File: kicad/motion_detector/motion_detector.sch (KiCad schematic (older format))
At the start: 20 parts, among them SW1 SW_Push, U1 MPU9250, U2 AE-FT234X, U3 pic16f18326, U4 tactile_sw, U5 EEPROM

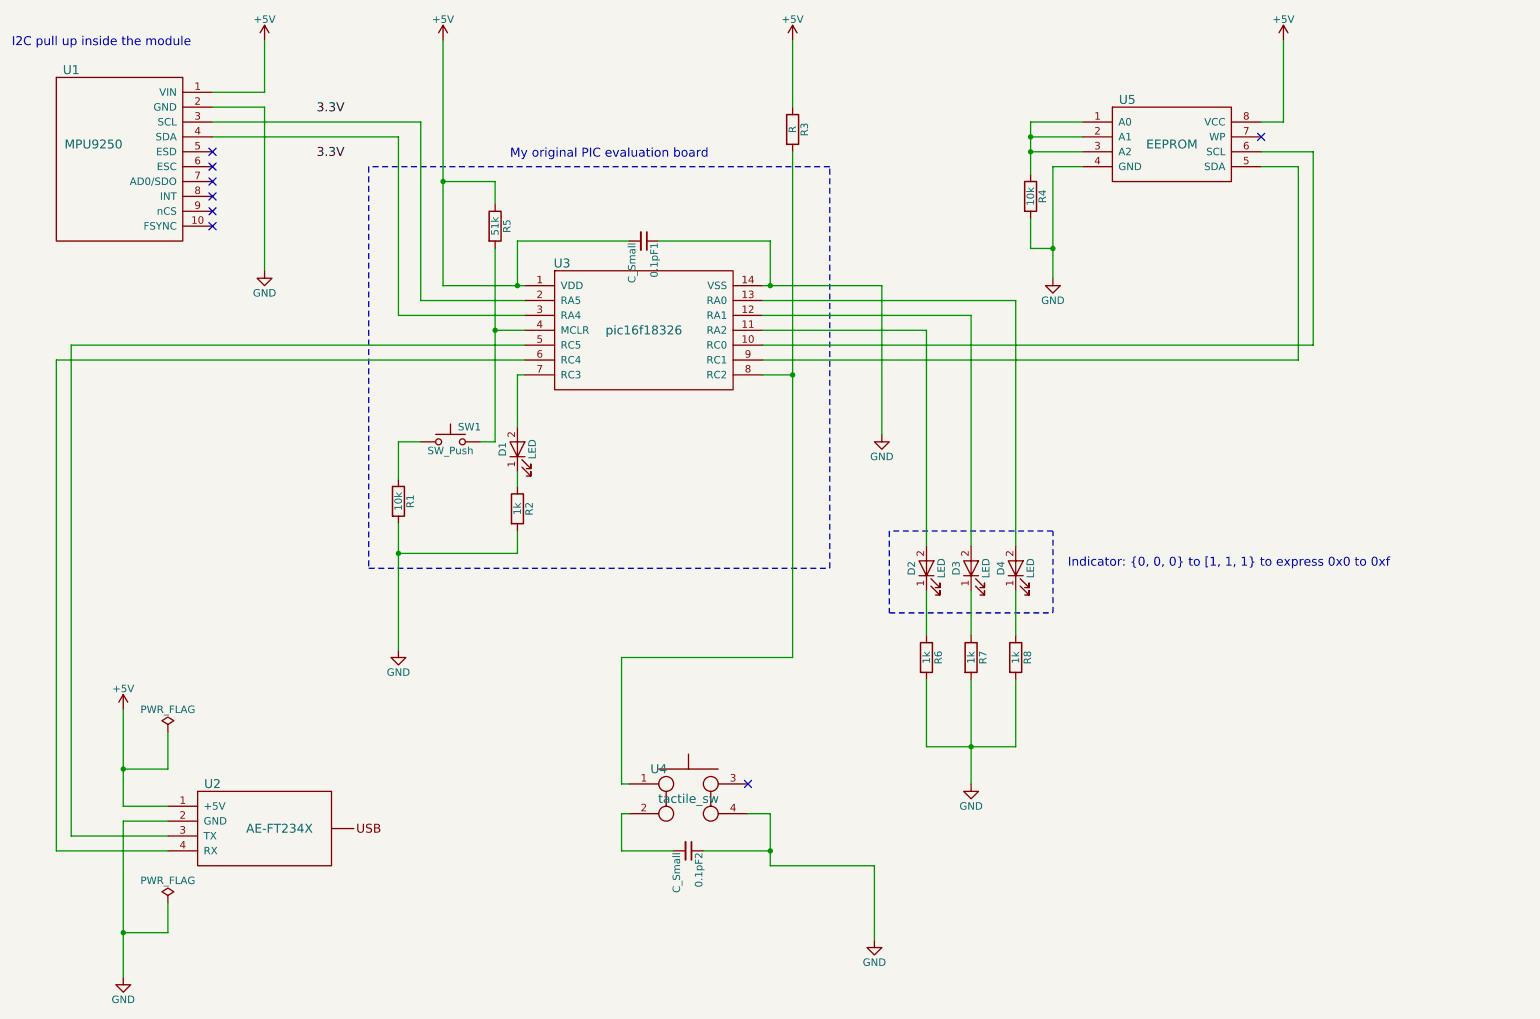
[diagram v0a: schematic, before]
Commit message: EEPROM test succeded
Atmel EEPROM page write and sequential read has been performed.
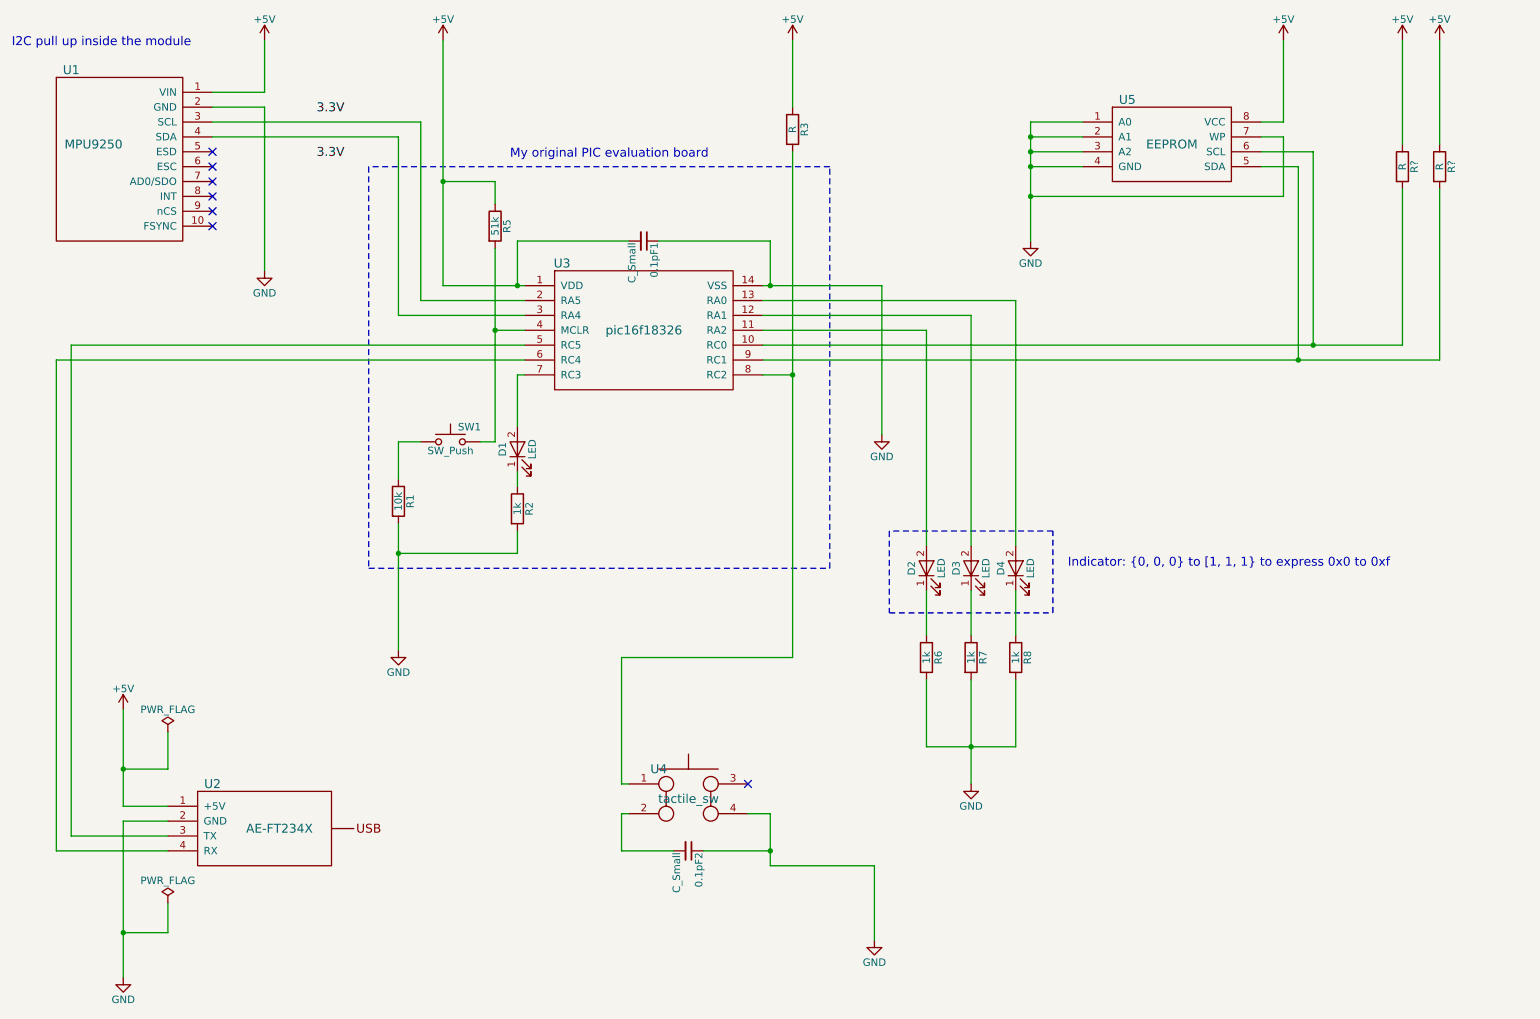
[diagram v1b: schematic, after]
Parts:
- removed R4: 10k, symbol R
- added R? (x2): R, symbol R
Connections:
- net +5V: now also R?.1, R?.1
- net GND: now also U5.1 (A0), U5.2 (A1), U5.3 (A2), U5.7 (WP)
- net at U3.10 (RC0), U5.6 (SCL): now also R?.2
- net at U3.9 (RC1), U5.5 (SDA): now also R?.2
- no-connect marks 8 -> 7
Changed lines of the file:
@@
 L GND #PWR11
 U 1 1 5B534DDB
-P 7750 2700
-F 0 "#PWR11" H 7750 2450 50  0001 C CNN
-F 1 "GND" H 7750 2550 50  0000 C CNN
-F 2 "" H 7750 2700 50  0001 C CNN
-F 3 "" H 7750 2700 50  0001 C CNN
-	1    7750 2700
-	1    0    0    -1
-$EndComp
-$Comp
-L R R4
-U 1 1 5B534E85
-P 7600 2150
-F 0 "R4" V 7680 2150 50  0000 C CNN
-F 1 "10k" V 7600 2150 50  0000 C CNN
-F 2 "" V 7530 2150 50  0001 C CNN
-F 3 "" H 7600 2150 50  0001 C CNN
-	1    7600 2150
+P 7600 2450
+F 0 "#PWR11" H 7600 2200 50  0001 C CNN
+F 1 "GND" H 7600 2300 50  0000 C CNN
+F 2 "" H 7600 2450 50  0001 C CNN
+F 3 "" H 7600 2450 50  0001 C CNN
+	1    7600 2450
 	1    0    0    -1
 $EndComp
@@
 Text Notes 4100 1900 0    60   ~ 0
 My original PIC evaluation board
-NoConn ~ 9150 1750
 NoConn ~ 5700 6100
 $Comp
@@
 	4000 3800 3900 3800
 Wire Wire Line
-	4000 2500 4000 3800
+	4000 2500 4000 3050
+Wire Wire Line
+	4000 3050 4000 3800
 Wire Wire Line
 	4000 3050 4200 3050
 Wire Wire Line
-	3350 4350 3350 5200
-Wire Wire Line
-	3650 1100 3650 2750
-Wire Wire Line
-	3650 2750 4200 2750
-Wire Wire Line
-	5800 2750 6600 2750
+	3350 4350 3350 4550
+Wire Wire Line
+	3350 4550 3350 5200
+Wire Wire Line
+	3650 1100 3650 2050
+Wire Wire Line
+	3650 2050 3650 2750
+Wire Wire Line
+	3650 2750 4150 2750
+Wire Wire Line
+	4150 2750 4200 2750
+Wire Wire Line
+	5800 2750 5850 2750
+Wire Wire Line
+	5850 2750 6600 2750
 Wire Wire Line
 	2100 1550 2450 1550
@@
 	5800 3150 9500 3150
 Wire Wire Line
+	9500 3150 10100 3150
+Wire Wire Line
 	5800 3250 9400 3250
+Wire Wire Line
+	9400 3250 10350 3250
 Wire Wire Line
 	2100 1650 3500 1650
@@
 	9300 1650 9300 1100
 Wire Wire Line
-	7950 1950 7750 1950
-Wire Wire Line
-	7750 1950 7750 2700
-Wire Wire Line
 	7600 1850 7950 1850
 Wire Wire Line
-	7600 1650 7600 2000
+	7600 1650 7600 1750
+Wire Wire Line
+	7600 1750 7600 1850
+Wire Wire Line
+	7600 1850 7600 1950
+Wire Wire Line
+	7600 1950 7600 2150
+Wire Wire Line
+	7600 2150 7600 2450
 Wire Wire Line
 	7950 1750 7600 1750
-Connection ~ 7600 1850
 Wire Wire Line
 	7950 1650 7600 1650
 Connection ~ 7600 1750
 Wire Wire Line
-	7600 2300 7600 2500
-Wire Wire Line
-	7600 2500 7750 2500
-Connection ~ 7750 2500
-Wire Wire Line
 	5850 6650 6550 6650
 Wire Wire Line
@@
 	1500 6250 1800 6250
 Wire Wire Line
-	1500 5600 1500 6250
+	1500 5600 1500 6000
+Wire Wire Line
+	1500 6000 1500 6250
 Wire Wire Line
 	1800 6350 1500 6350
 Wire Wire Line
-	1500 6350 1500 7400
+	1500 6350 1500 7100
+Wire Wire Line
+	1500 7100 1500 7400
 Wire Wire Line
 	6600 2750 6600 3750
@@
 	5700 6300 5850 6300
 Wire Wire Line
-	5850 6300 5850 6650
+	5850 6300 5850 6550
+Wire Wire Line
+	5850 6550 5850 6650
 Connection ~ 4000 3050
 Wire Wire Line
@@
 	6900 5400 6900 5850
 Wire Wire Line
-	6900 5850 7500 5850
-Wire Wire Line
-	7200 5400 7200 6100
+	6900 5850 7200 5850
+Wire Wire Line
+	7200 5850 7500 5850
+Wire Wire Line
+	7200 5400 7200 5850
+Wire Wire Line
+	7200 5850 7200 6100
 Connection ~ 7200 5850
 Wire Wire Line
@@
 	5800 3350 6000 3350
 Wire Wire Line
-	6000 1850 6000 5250
+	6000 1850 6000 3350
+Wire Wire Line
+	6000 3350 6000 5250
 Wire Wire Line
 	6000 5250 4850 5250
@@
 	4850 6100 4900 6100
 Connection ~ 6000 3350
+$Comp
+L R R?
+U 1 1 5B56667D
+P 10100 1950
+F 0 "R?" V 10180 1950 50  0000 C CNN
+F 1 "R" V 10100 1950 50  0000 C CNN
+F 2 "" V 10030 1950 50  0001 C CNN
+F 3 "" H 10100 1950 50  0001 C CNN
+	1    10100 1950
+	1    0    0    -1
+$EndComp
+$Comp
+L R R?
+U 1 1 5B5666DA
+P 10350 1950
+F 0 "R?" V 10430 1950 50  0000 C CNN
+F 1 "R" V 10350 1950 50  0000 C CNN
+F 2 "" V 10280 1950 50  0001 C CNN
+F 3 "" H 10350 1950 50  0001 C CNN
+	1    10350 1950
+	1    0    0    -1
+$EndComp
+Wire Wire Line
+	10100 3150 10100 2100
+Connection ~ 9500 3150
+Wire Wire Line
+	10350 3250 10350 2100
+Connection ~ 9400 3250
+$Comp
+L +5V #PWR?
+U 1 1 5B56687B
+P 10100 1100
+F 0 "#PWR?" H 10100 950 50  0001 C CNN
+F 1 "+5V" H 10100 1240 50  0000 C CNN
+F 2 "" H 10100 1100 50  0001 C CNN
+F 3 "" H 10100 1100 50  0001 C CNN
+	1    10100 1100
+	1    0    0    -1
+$EndComp
+$Comp
+L +5V #PWR?
+U 1 1 5B5668BB
+P 10350 1100
+F 0 "#PWR?" H 10350 950 50  0001 C CNN
+F 1 "+5V" H 10350 1240 50  0000 C CNN
+F 2 "" H 10350 1100 50  0001 C CNN
+F 3 "" H 10350 1100 50  0001 C CNN
+	1    10350 1100
+	1    0    0    -1
+$EndComp
+Wire Wire Line
+	10100 1100 10100 1800
+Wire Wire Line
+	10350 1100 10350 1800
+Wire Wire Line
+	7600 1950 7950 1950
+Connection ~ 7600 1950
+Connection ~ 7600 1850
+Wire Wire Line
+	9150 1750 9300 1750
+Wire Wire Line
+	9300 1750 9300 2150
+Wire Wire Line
+	9300 2150 7600 2150
+Connection ~ 7600 2150
 $EndSCHEMATC

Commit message: update
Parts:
- gave numbers to parts that had none: 2
- renumbered R5 to R2, R2 to R3, R3 to R4, R6 to R5, R7 to R6, R8 to R7
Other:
- note added: "256kbits"
- note added: "400kHz"
- note added: "Or connect a mobile battery 5V\nto use this system in a stand alone mode"
- note added: "Push to start measurement for 3 sec"
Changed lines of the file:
@@
 encoding utf-8
 Sheet 1 1
-Title "Motion detector"
-Date "2018-07-21"
-Rev "v0.1"
+Title "Motion sensor"
+Date "2018-07-24"
+Rev "v0.2"
 Comp "https://github.com/araobp"
 Comment1 ""
 Comment2 ""
-Comment3 ""
-Comment4 ""
+Comment3 "Atmel 256kbits EEPROM (I2C)"
+Comment4 "TDK InvenSense nine-axis sensor (I2C)"
 $EndDescr
 $Comp
@@
 $EndComp
 $Comp
-L R R2
+L R R3
 U 1 1 5B533F63
 P 4150 4250
-F 0 "R2" V 4230 4250 50  0000 C CNN
+F 0 "R3" V 4230 4250 50  0000 C CNN
 F 1 "1k" V 4150 4250 50  0000 C CNN
 F 2 "" V 4080 4250 50  0001 C CNN
@@
 NoConn ~ 5700 6100
 $Comp
-L R R5
+L R R2
 U 1 1 5B53AB68
 P 4000 2350
-F 0 "R5" V 4080 2350 50  0000 C CNN
+F 0 "R2" V 4080 2350 50  0000 C CNN
 F 1 "51k" V 4000 2350 50  0000 C CNN
 F 2 "" V 3930 2350 50  0001 C CNN
@@
 $EndComp
 $Comp
-L R R3
+L R R4
 U 1 1 5B53B926
 P 6000 1700
-F 0 "R3" V 6080 1700 50  0000 C CNN
+F 0 "R4" V 6080 1700 50  0000 C CNN
 F 1 "R" V 6000 1700 50  0000 C CNN
 F 2 "" V 5930 1700 50  0001 C CNN
@@
 $EndComp
 $Comp
-L R R6
+L R R5
 U 1 1 5B53F808
 P 6900 5250
-F 0 "R6" V 6980 5250 50  0000 C CNN
+F 0 "R5" V 6980 5250 50  0000 C CNN
 F 1 "1k" V 6900 5250 50  0000 C CNN
 F 2 "" V 6830 5250 50  0001 C CNN
@@
 $EndComp
 $Comp
-L R R7
+L R R6
 U 1 1 5B53F875
 P 7200 5250
-F 0 "R7" V 7280 5250 50  0000 C CNN
+F 0 "R6" V 7280 5250 50  0000 C CNN
 F 1 "1k" V 7200 5250 50  0000 C CNN
 F 2 "" V 7130 5250 50  0001 C CNN
@@
 $EndComp
 $Comp
-L R R8
+L R R7
 U 1 1 5B53F8B4
 P 7500 5250
-F 0 "R8" V 7580 5250 50  0000 C CNN
+F 0 "R7" V 7580 5250 50  0000 C CNN
 F 1 "1k" V 7500 5250 50  0000 C CNN
 F 2 "" V 7430 5250 50  0001 C CNN
@@
 Connection ~ 6000 3350
 $Comp
-L R R?
+L R R8
 U 1 1 5B56667D
 P 10100 1950
-F 0 "R?" V 10180 1950 50  0000 C CNN
+F 0 "R8" V 10180 1950 50  0000 C CNN
 F 1 "R" V 10100 1950 50  0000 C CNN
 F 2 "" V 10030 1950 50  0001 C CNN
@@
 $EndComp
 $Comp
-L R R?
+L R R9
 U 1 1 5B5666DA
 P 10350 1950
-F 0 "R?" V 10430 1950 50  0000 C CNN
+F 0 "R9" V 10430 1950 50  0000 C CNN
 F 1 "R" V 10350 1950 50  0000 C CNN
 F 2 "" V 10280 1950 50  0001 C CNN
@@
 Connection ~ 9400 3250
 $Comp
-L +5V #PWR?
+L +5V #PWR13
 U 1 1 5B56687B
 P 10100 1100
-F 0 "#PWR?" H 10100 950 50  0001 C CNN
+F 0 "#PWR13" H 10100 950 50  0001 C CNN
 F 1 "+5V" H 10100 1240 50  0000 C CNN
 F 2 "" H 10100 1100 50  0001 C CNN
@@
 $EndComp
 $Comp
-L +5V #PWR?
+L +5V #PWR14
 U 1 1 5B5668BB
 P 10350 1100
-F 0 "#PWR?" H 10350 950 50  0001 C CNN
+F 0 "#PWR14" H 10350 950 50  0001 C CNN
 F 1 "+5V" H 10350 1240 50  0000 C CNN
 F 2 "" H 10350 1100 50  0001 C CNN
@@
 	9300 2150 7600 2150
 Connection ~ 7600 2150
+Text Notes 2350 6100 0    60   ~ 0
+Or connect a mobile battery 5V\nto use this system in a stand alone mode
+Text Notes 8300 3100 0    60   ~ 0
+400kHz
+Text Notes 3200 1600 0    60   ~ 0
+400kHz
+Text Notes 8450 1500 0    60   ~ 0
+256kbits
+Text Notes 4950 5800 0    60   ~ 0
+Push to start measurement for 3 sec
 $EndSCHEMATC
